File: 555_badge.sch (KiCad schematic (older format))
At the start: 15 parts, among them Q1 2N3904, U1 7555

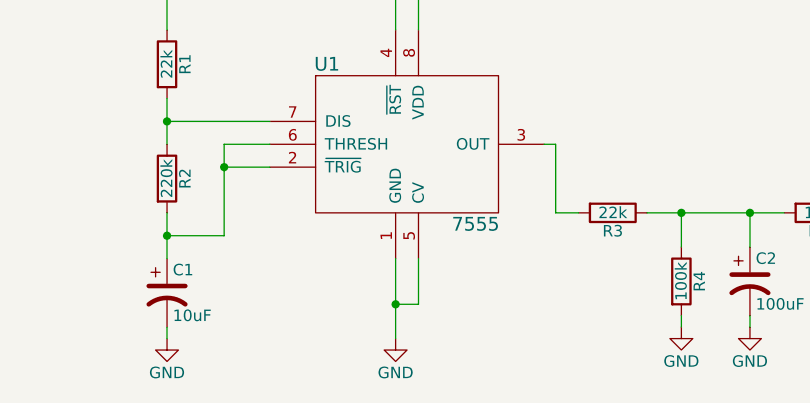
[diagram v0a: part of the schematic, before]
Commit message: v00a. Flipped LEDs, disconnected CV on 7555, widened slot.
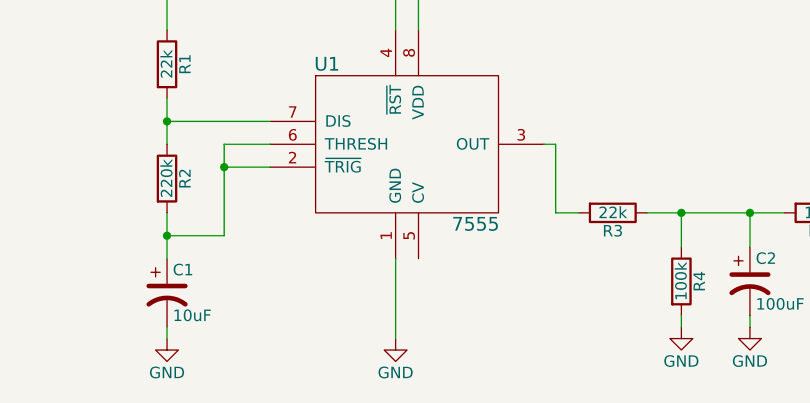
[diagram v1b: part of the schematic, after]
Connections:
- net GND: no longer U1.5 (CV)
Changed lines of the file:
@@
 Title "555 Badge"
 Date "2017-11-26"
-Rev "v01"
+Rev "v00a"
 Comp "Shawn Hymel"
 Comment1 ""
@@
 	5500 4100 5500 4450
 Wire Wire Line
-	5600 4100 5600 4300
-Wire Wire Line
-	5600 4300 5500 4300
-Connection ~ 5500 4300
-Wire Wire Line
 	6150 3600 6200 3600

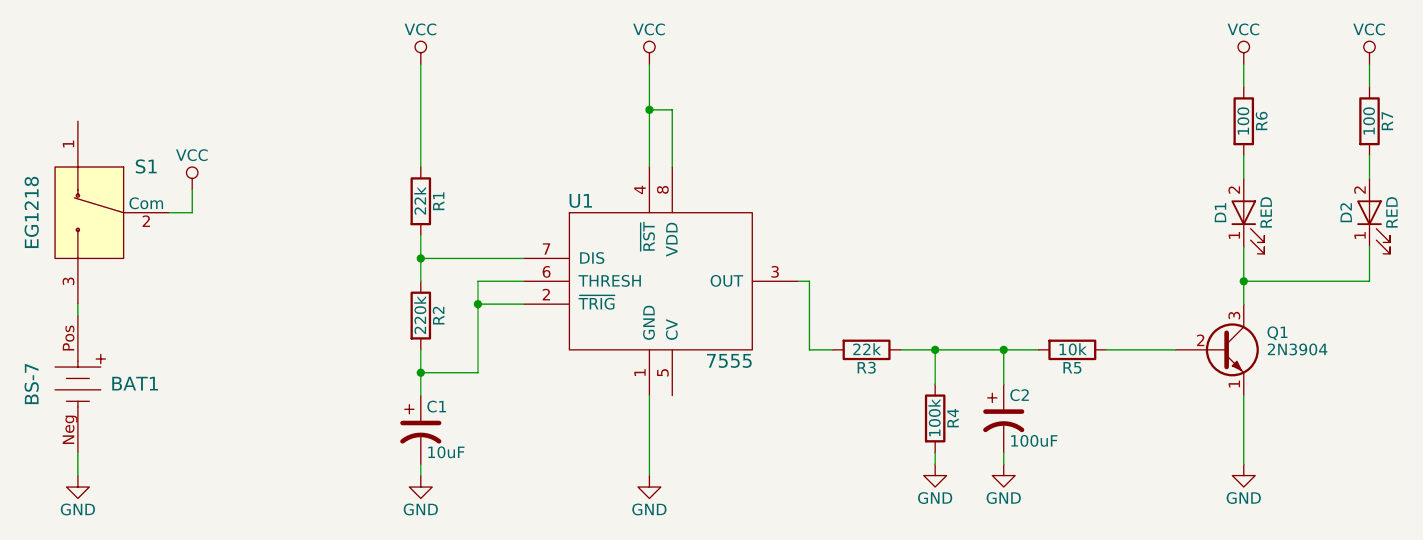
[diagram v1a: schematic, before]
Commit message: Changed R2 to 330k
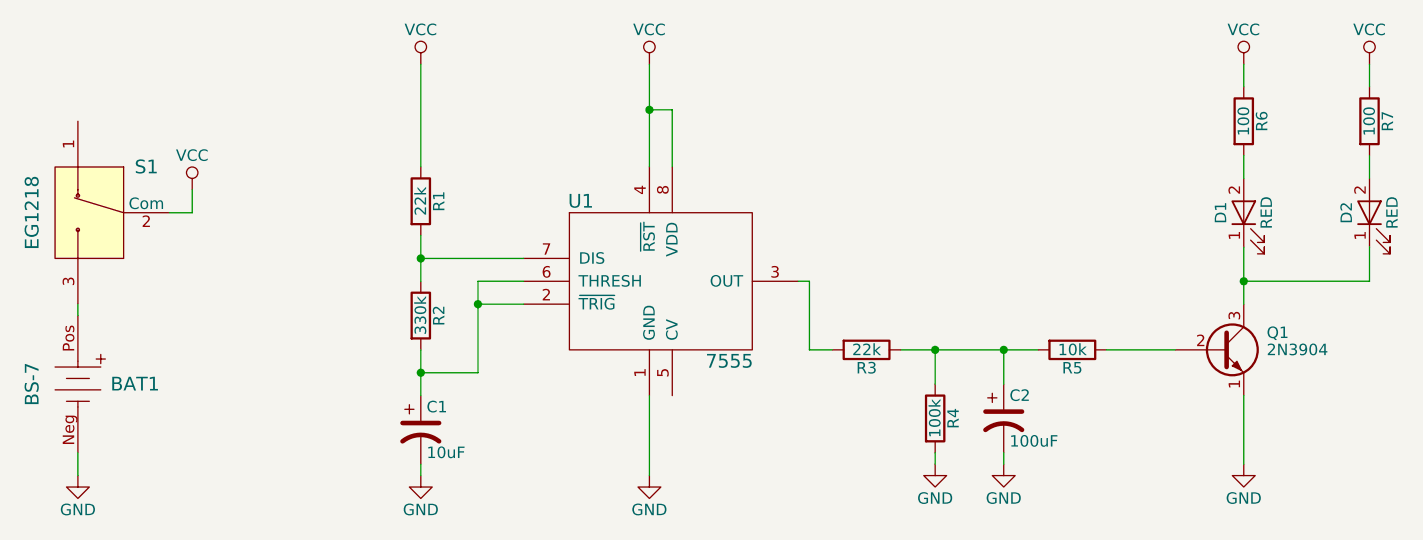
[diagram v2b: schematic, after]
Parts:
- R2: value 220k -> 330k
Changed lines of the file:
@@
 P 4500 3750
 F 0 "R2" V 4580 3750 50  0000 C CNN
-F 1 "220k" V 4500 3750 50  0000 C CNN
+F 1 "330k" V 4500 3750 50  0000 C CNN
 F 2 "Resistors_THT:R_Axial_DIN0207_L6.3mm_D2.5mm_P7.62mm_Horizontal" V 4430 3750 50  0001 C CNN
 F 3 "" H 4500 3750 50  0001 C CNN
